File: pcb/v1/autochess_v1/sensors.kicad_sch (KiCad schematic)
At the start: 144 parts, among them Q1 BS170, Q2 BS170, Q3 BS170, Q4 BS170, Q5 BS170, Q6 BS170, Q7 BS170, Q8 BS170, U10 DRV5033A, U11 DRV5033A, U12 DRV5033A, U13 DRV5033A, U14 DRV5033A, U15 DRV5033A, U16 DRV5033A, U17 DRV5033A, U18 DRV5033A, U19 DRV5033A, U2 DRV5033A, U20 DRV5033A, U21 DRV5033A, U22 DRV5033A, U23 DRV5033A, U24 DRV5033A, U25 DRV5033A, U26 DRV5033A, U27 DRV5033A, U28 DRV5033A, U29 DRV5033A, U3 DRV5033A, U30 DRV5033A, U31 DRV5033A, U32 DRV5033A, U33 DRV5033A, U34 DRV5033A, U35 DRV5033A, U36 DRV5033A, U37 DRV5033A, U38 DRV5033A, U39 DRV5033A, U4 DRV5033A, U40 DRV5033A, U41 DRV5033A, U42 DRV5033A, U43 DRV5033A, U44 DRV5033A, U45 DRV5033A, U46 DRV5033A, U47 DRV5033A, U48 DRV5033A, U49 DRV5033A, U5 DRV5033A, U50 DRV5033A, U51 DRV5033A, U52 DRV5033A, U53 DRV5033A, U54 DRV5033A, U55 DRV5033A, U56 DRV5033A, U57 DRV5033A, U58 DRV5033A, U59 DRV5033A, U6 DRV5033A, U60 DRV5033A, U61 DRV5033A, U62 DRV5033A, U63 DRV5033A, U64 DRV5033A, U65 DRV5033A, U7 DRV5033A, U8 DRV5033A, U9 DRV5033A

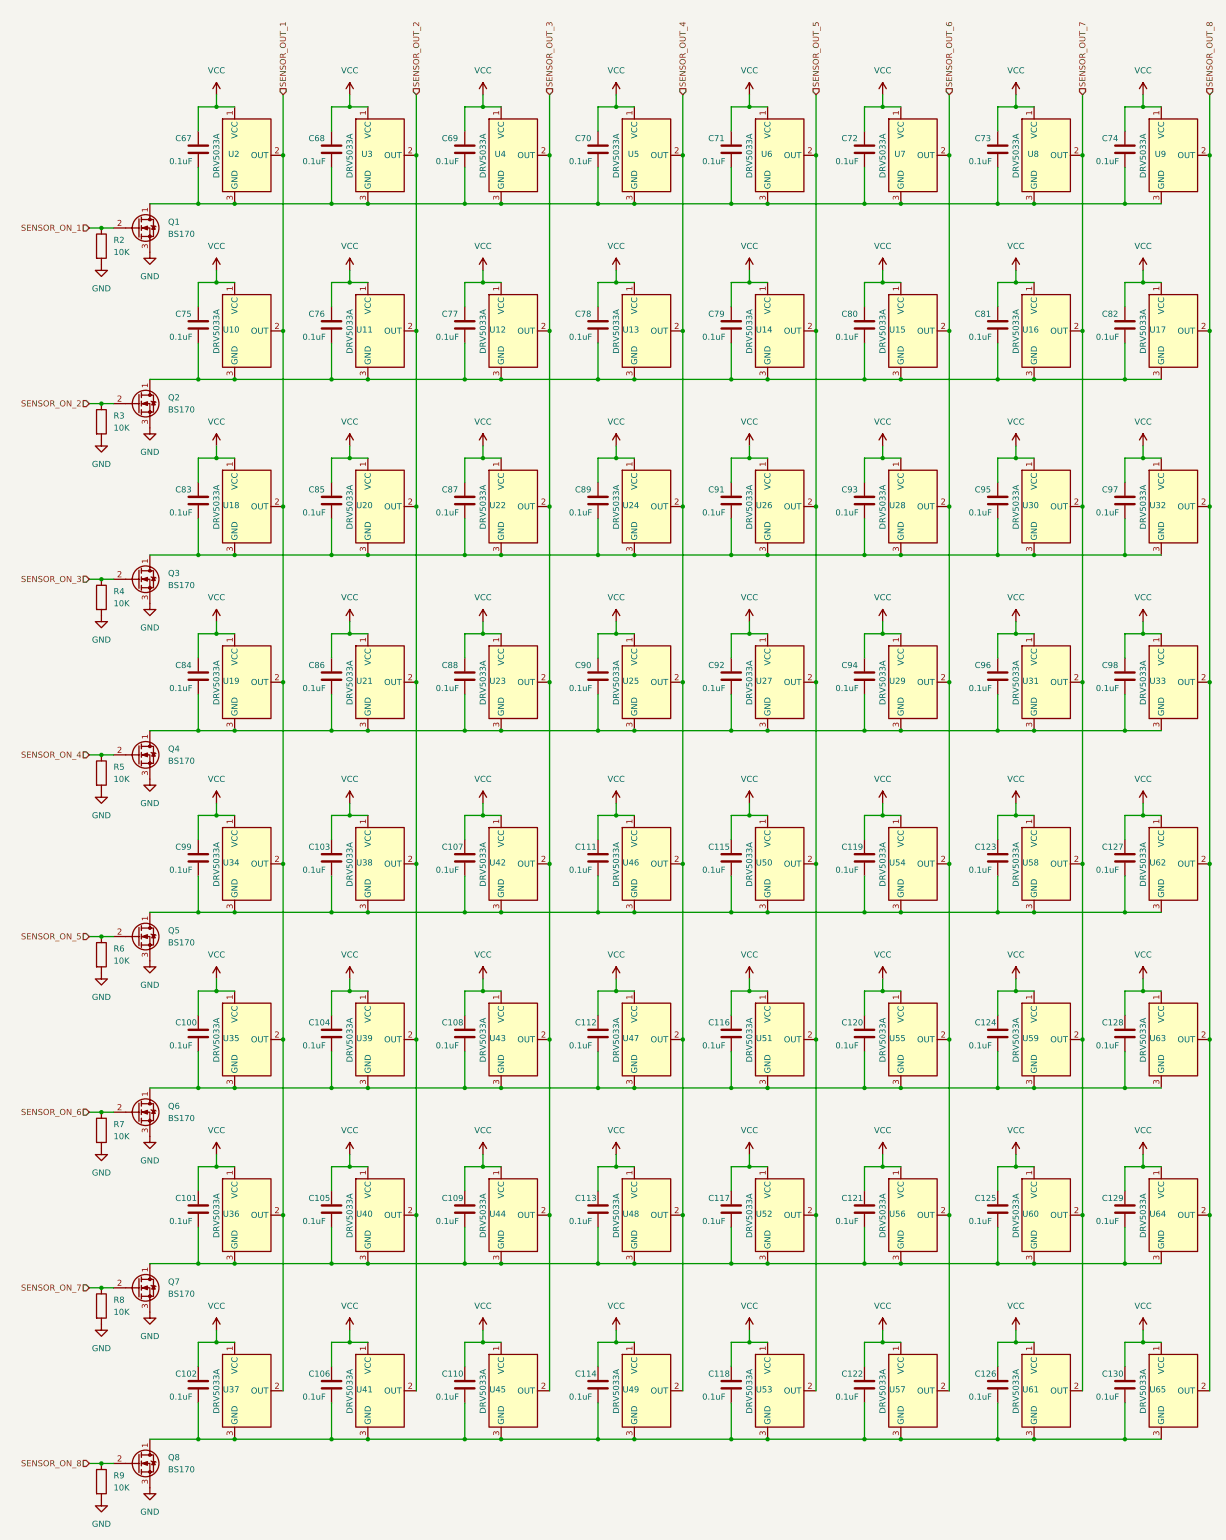
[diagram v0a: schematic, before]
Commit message: Finish the schematic draft, start pcb layout
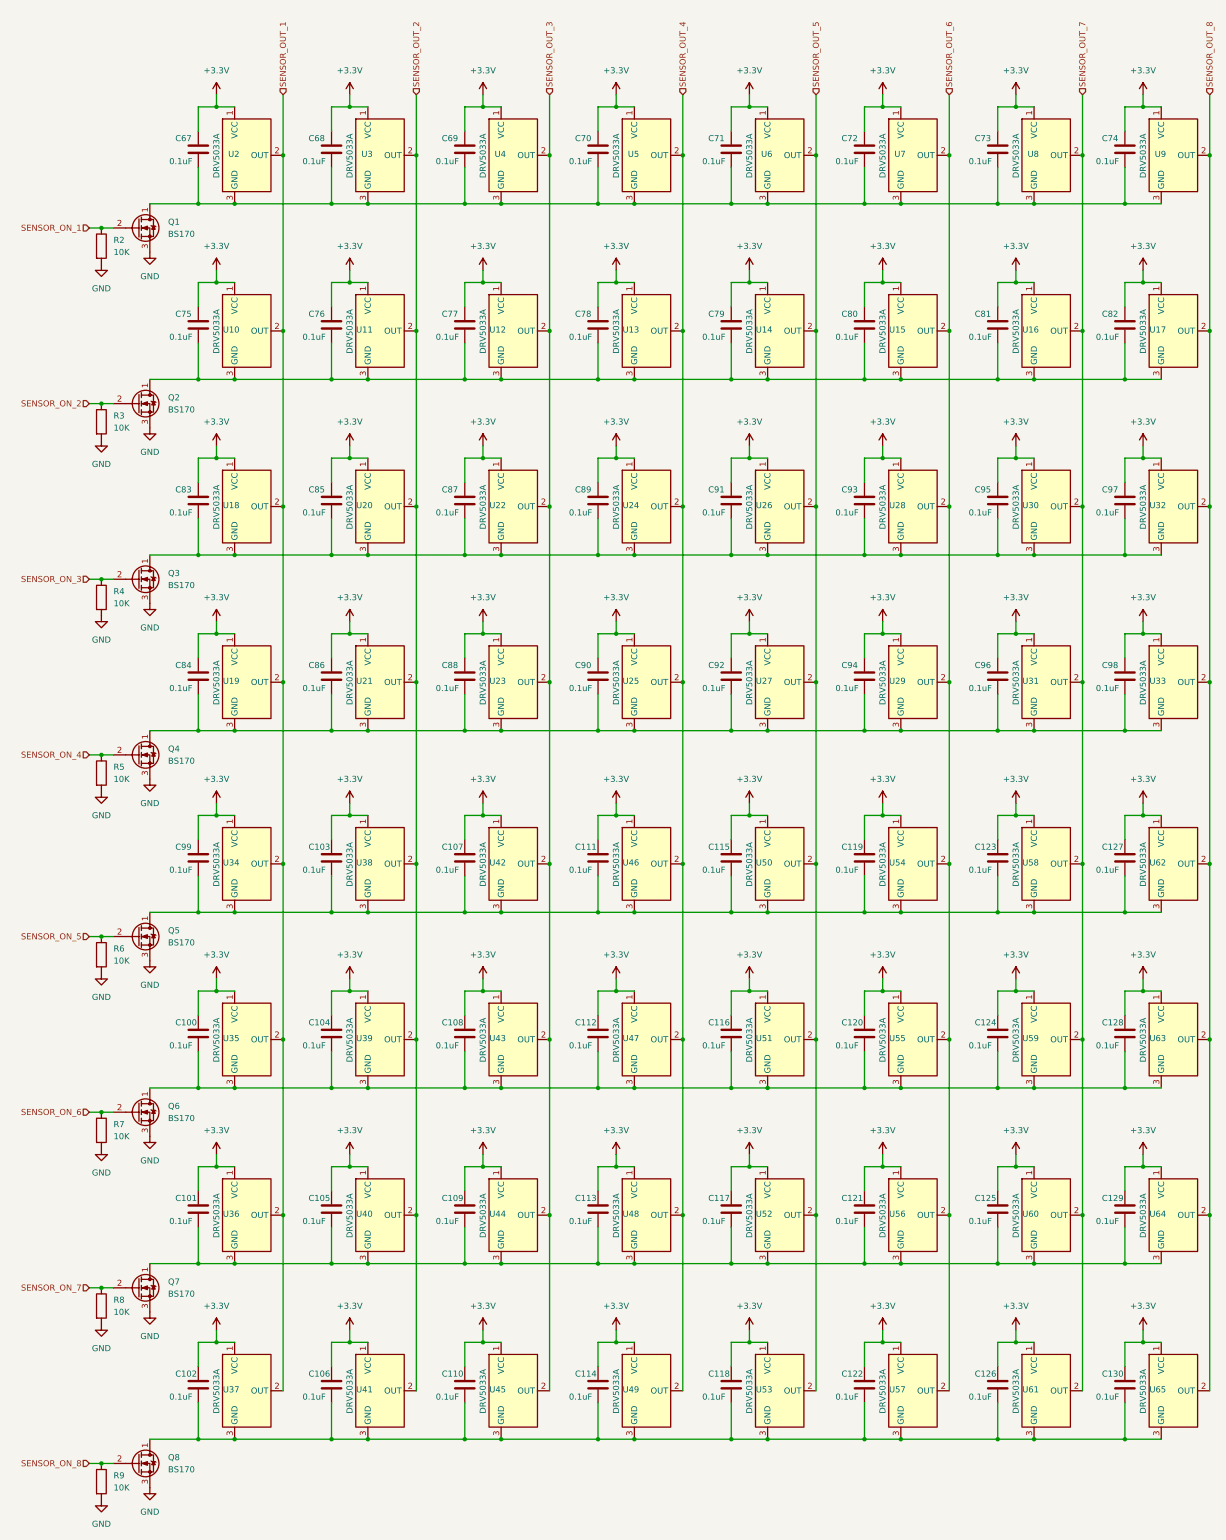
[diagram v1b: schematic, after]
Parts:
- C100, C101, C102, C103, C104, C105, C106, C107, C108, C109, C110, C111, C112, C113, C114, C115, C116, C117, C118, C119, C120, C121, C122, C123, C124, C125, C126, C127, C128, C129, C130, C67, C68, C69, C70, C71, C72, C73, C74, C75, C76, C77, C78, C79, C80, C81, C82, C83, C84, C85, C86, C87, C88, C89, C90, C91, C92, C93, C94, C95, C96, C97, C98, C99: footprint (none) -> Capacitor_SMD:C_1206_3216Metric_Pad1.33x1.80mm_HandSolder
- R2, R3, R4, R5, R6, R7, R8, R9: footprint (none) -> Resistor_SMD:R_1206_3216Metric_Pad1.30x1.75mm_HandSolder
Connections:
- net VCC renamed +3.3V

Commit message: Continue laying out the PCB
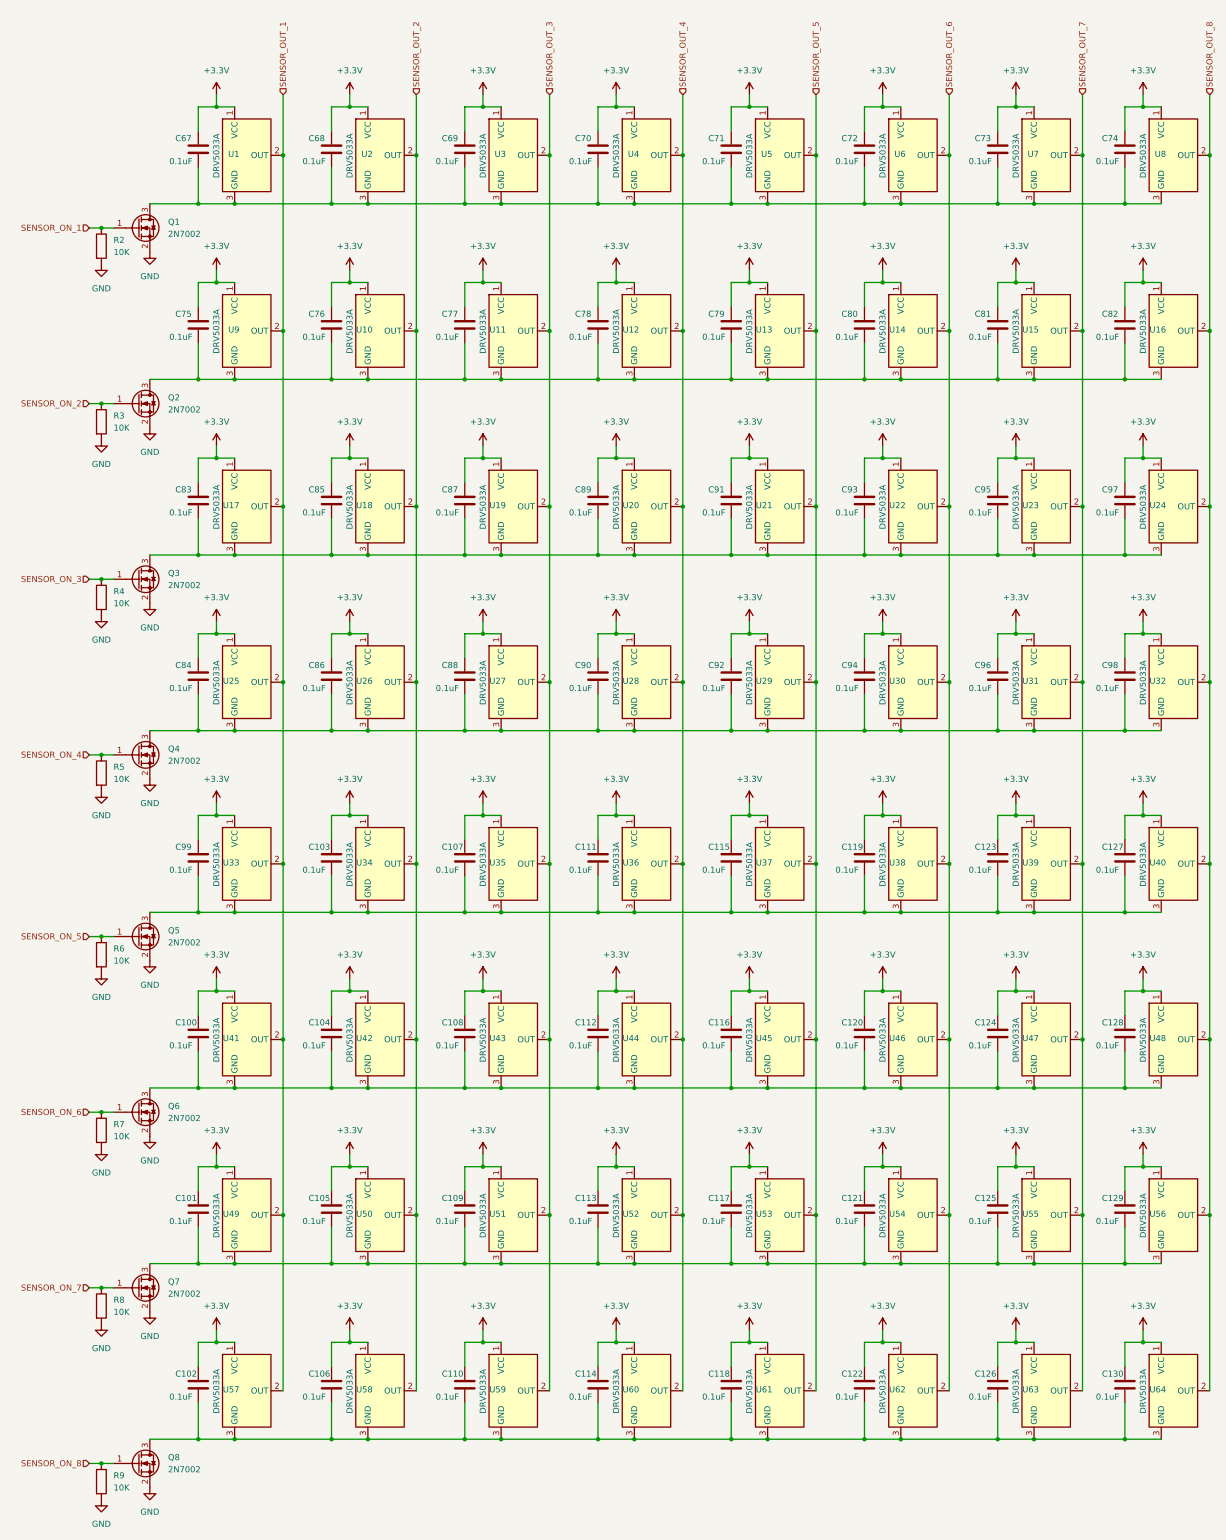
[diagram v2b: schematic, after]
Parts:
- removed Q1, Q2, Q3, Q4, Q5, Q6, Q7, Q8: BS170, Package_TO_SOT_THT:TO-92_Inline, symbol Transistor_FET:BS170
- added Q1, Q2, Q3, Q4, Q5, Q6, Q7, Q8: 2N7002, Package_TO_SOT_SMD:SOT-23, symbol Transistor_FET:2N7002
- renumbered U2 to U1, U11 to U10, U12 to U11, U13 to U12, U14 to U13, U15 to U14, U16 to U15, U17 to U16, U18 to U17, U20 to U18, U22 to U19, U3 to U2, U24 to U20, U26 to U21, U28 to U22, U30 to U23, U32 to U24, U19 to U25, U21 to U26, U23 to U27, U25 to U28, U27 to U29, U4 to U3, U29 to U30, U33 to U32, U34 to U33, U38 to U34, U42 to U35, U46 to U36, U50 to U37, U54 to U38, U58 to U39, U5 to U4, U62 to U40, U35 to U41, U39 to U42, U47 to U44, U51 to U45, U55 to U46, U59 to U47, U63 to U48, U36 to U49, U6 to U5, U40 to U50, U44 to U51, U48 to U52, U52 to U53, U56 to U54, U60 to U55, U64 to U56, U37 to U57, U41 to U58, U45 to U59, U7 to U6, U49 to U60, U53 to U61, U57 to U62, U61 to U63, U65 to U64, U8 to U7, U9 to U8, U10 to U9
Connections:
- net GND: now also Q1.2 (S), Q2.2 (S), Q3.2 (S), Q4.2 (S), Q5.2 (S), Q6.2 (S), Q7.2 (S), Q8.2 (S)
- net SENSOR_ON_1: now also Q1.1 (G)
- net SENSOR_ON_2: now also Q2.1 (G)
- net SENSOR_ON_3: now also Q3.1 (G)
- net SENSOR_ON_4: now also Q4.1 (G)
- net SENSOR_ON_5: now also Q5.1 (G)
- net SENSOR_ON_6: now also Q6.1 (G)
- net SENSOR_ON_7: now also Q7.1 (G)
- net SENSOR_ON_8: now also Q8.1 (G)
- net at C103.2, C107.2, C111.2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: now also Q5.3 (D)
- net at C67.2, C68.2, C69.2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: now also Q1.3 (D)
- net at C83.2, C85.2, C87.2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: now also Q3.3 (D)
- net at C75.2, C76.2, C77.2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: now also Q2.3 (D)
- net at C84.2, C86.2, C88.2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: now also Q4.3 (D)
- net at C102.2, C106.2, C110.2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: now also Q8.3 (D)
- net at C100.2, C104.2, C108.2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: now also Q6.3 (D)
- net at C101.2, C105.2, C109.2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: now also Q7.3 (D)

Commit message: Continue placing
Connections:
- net +3.3V: now also C67.2; no longer C67.1
- net at C68.2, C69.2, C70.2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: now also C67.1; no longer C67.2
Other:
- moved on the sheet: C67
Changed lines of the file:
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@@
 	(symbol
 		(lib_id "Device:C")
-		(at 58.42 58.42 0)
+		(at 58.42 58.42 180)
 		(unit 1)
 		(body_style 1)
@@
 		(in_pos_files yes)
 		(dnp no)
-		(fields_autoplaced yes)
 		(property "Reference" "C67"
-			(at 53.594 56.134 0)
+			(at 52.07 56.134 0)
 			(show_name no)
 			(do_not_autoplace no)
@@
 					(size 1.27 1.27)
 				)
-				(justify left)
+				(justify right)
 			)
 		)
 		(property "Value" "0.1uF"
-			(at 52.324 60.96 0)
+			(at 51.562 61.214 0)
 			(show_name no)
 			(do_not_autoplace no)
@@
 					(size 1.27 1.27)
 				)
-				(justify left)
+				(justify right)
 			)
 		)
 		(property "Footprint" "Capacitor_SMD:C_1206_3216Metric_Pad1.33x1.80mm_HandSolder"
-			(at 59.3852 62.23 0)
+			(at 57.4548 54.61 0)
 			(hide yes)
 			(show_name no)

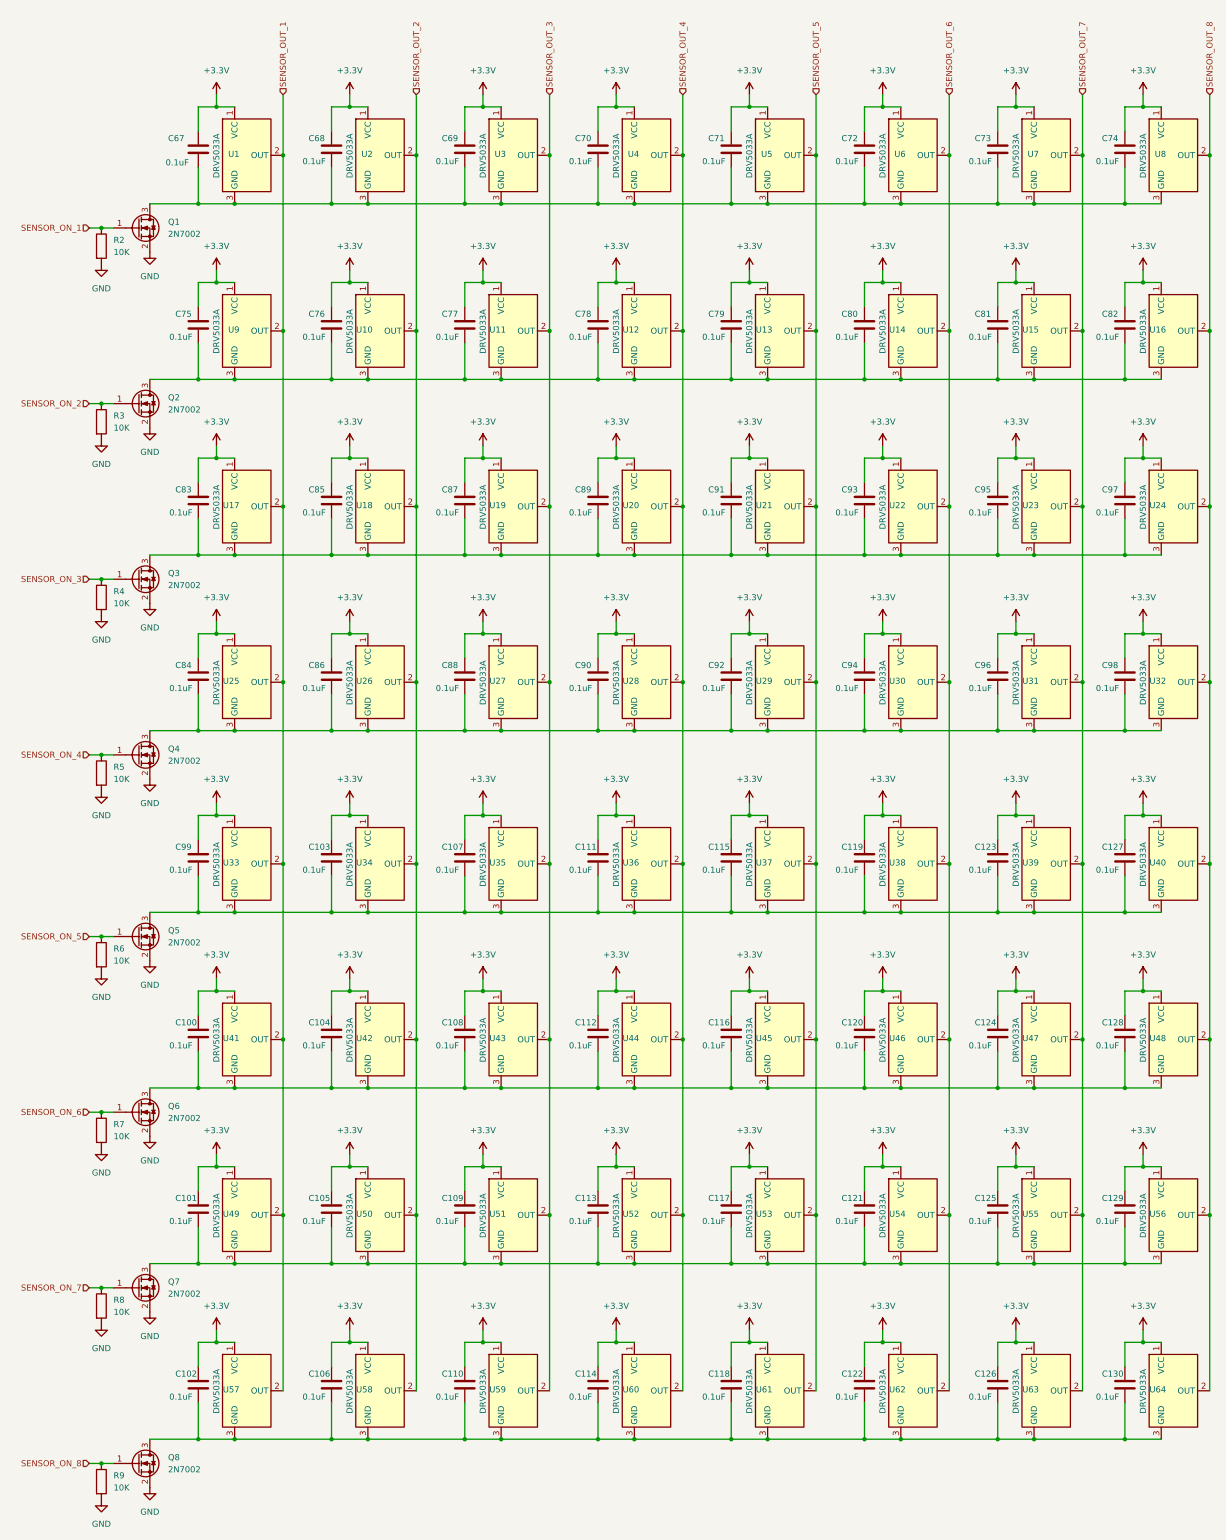
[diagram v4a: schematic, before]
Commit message: Place most components
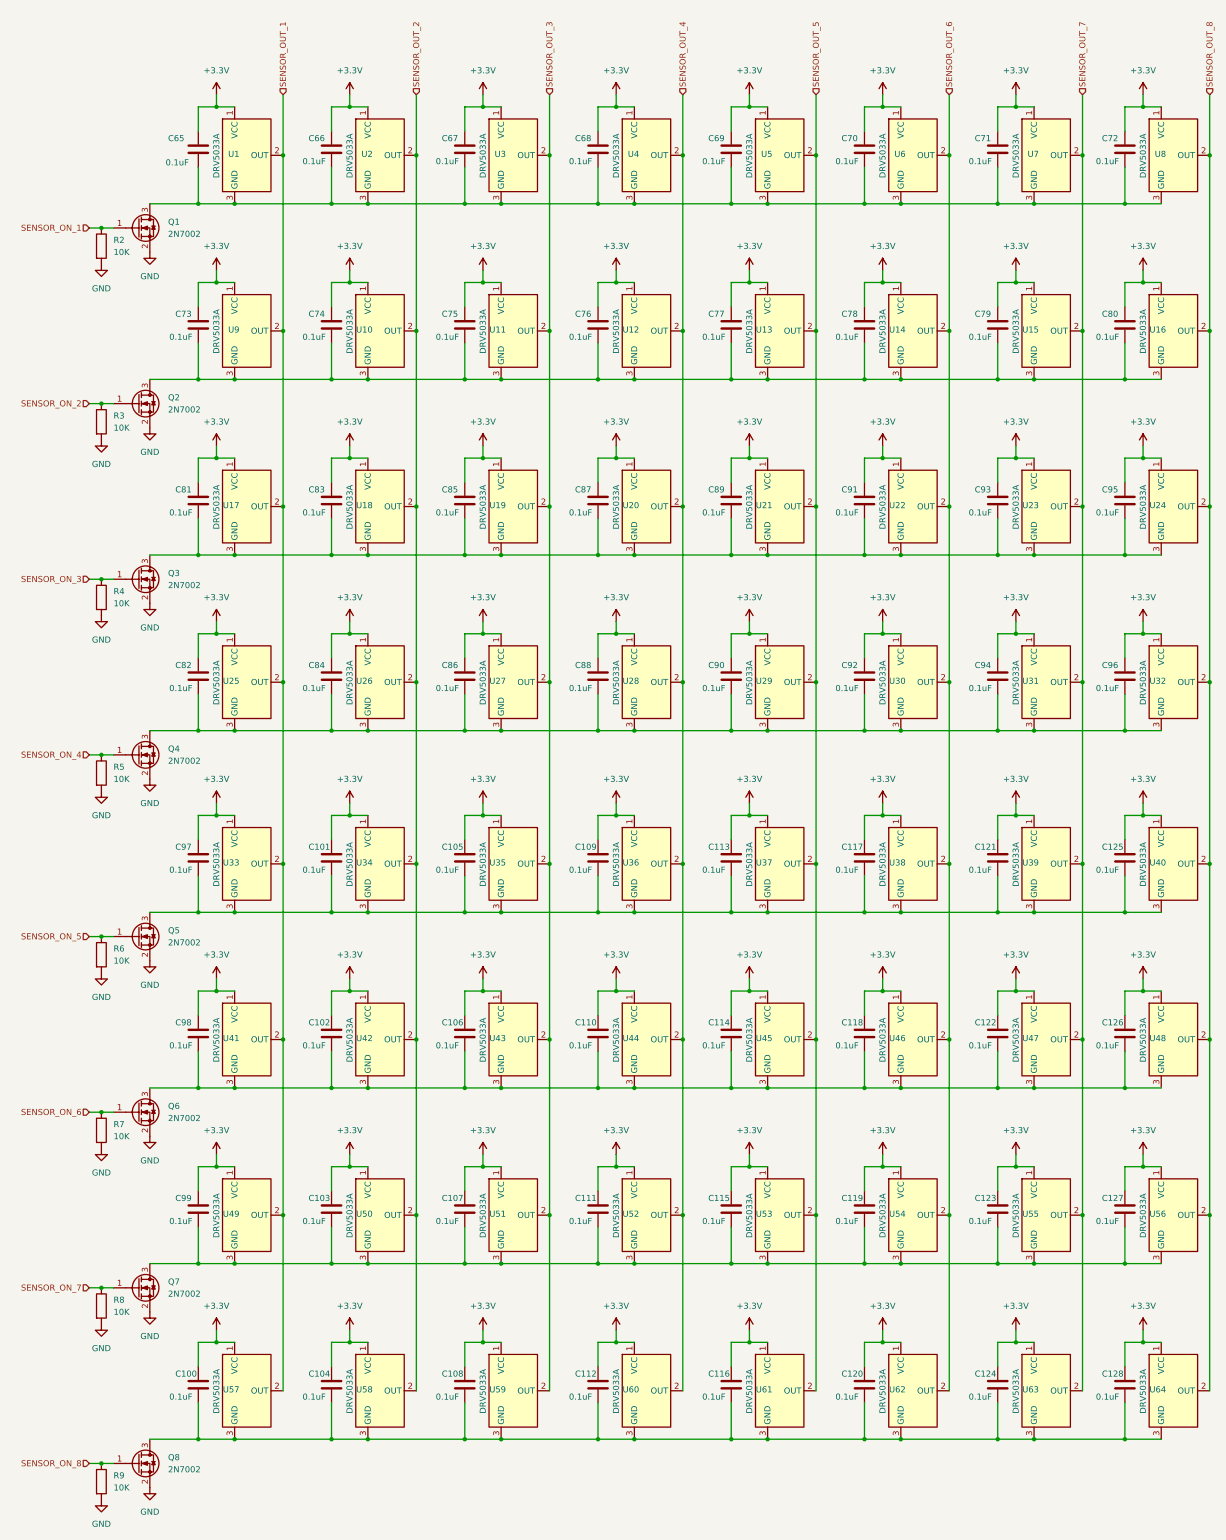
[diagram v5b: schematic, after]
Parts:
- renumbered C102 to C100, C103 to C101, C104 to C102, C105 to C103, C106 to C104, C107 to C105, C108 to C106, C109 to C107, C110 to C108, C111 to C109, C112 to C110, C113 to C111, C114 to C112, C115 to C113, C116 to C114, C117 to C115, C118 to C116, C119 to C117, C120 to C118, C121 to C119, C122 to C120, C123 to C121, C124 to C122, C125 to C123, C126 to C124, C127 to C125, C128 to C126, C129 to C127, C130 to C128, C67 to C65, C68 to C66, C69 to C67, C70 to C68, C71 to C69, C72 to C70, C73 to C71, C74 to C72, C75 to C73, C76 to C74, C77 to C75, C78 to C76, C79 to C77, C80 to C78, C81 to C79, C82 to C80, C83 to C81, C84 to C82, C85 to C83, C86 to C84, C87 to C85, C88 to C86, C89 to C87, C90 to C88, C91 to C89, C92 to C90, C93 to C91, C94 to C92, C95 to C93, C96 to C94, C97 to C95, C98 to C96, C99 to C97, C100 to C98, C101 to C99
